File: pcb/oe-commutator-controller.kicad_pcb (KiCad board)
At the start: 4 copper layers, 43 x 95 mm, 93 parts, among them J1 0015910100, J2 USB4110-GF-A, J3 1719730004, SW1 SW_Push, U1 W25Q128JVS, U2 RP2040, U3 NCP1117-3.3_SOT223, U4 CAP1296-x-AIA, U5 PTN04050CAZ, U6 LTC4425, U7 TMC2130-LA, U8 IS31FL3193, Y1 ABM8AIG-12.000MHZ-12-2Z-T3

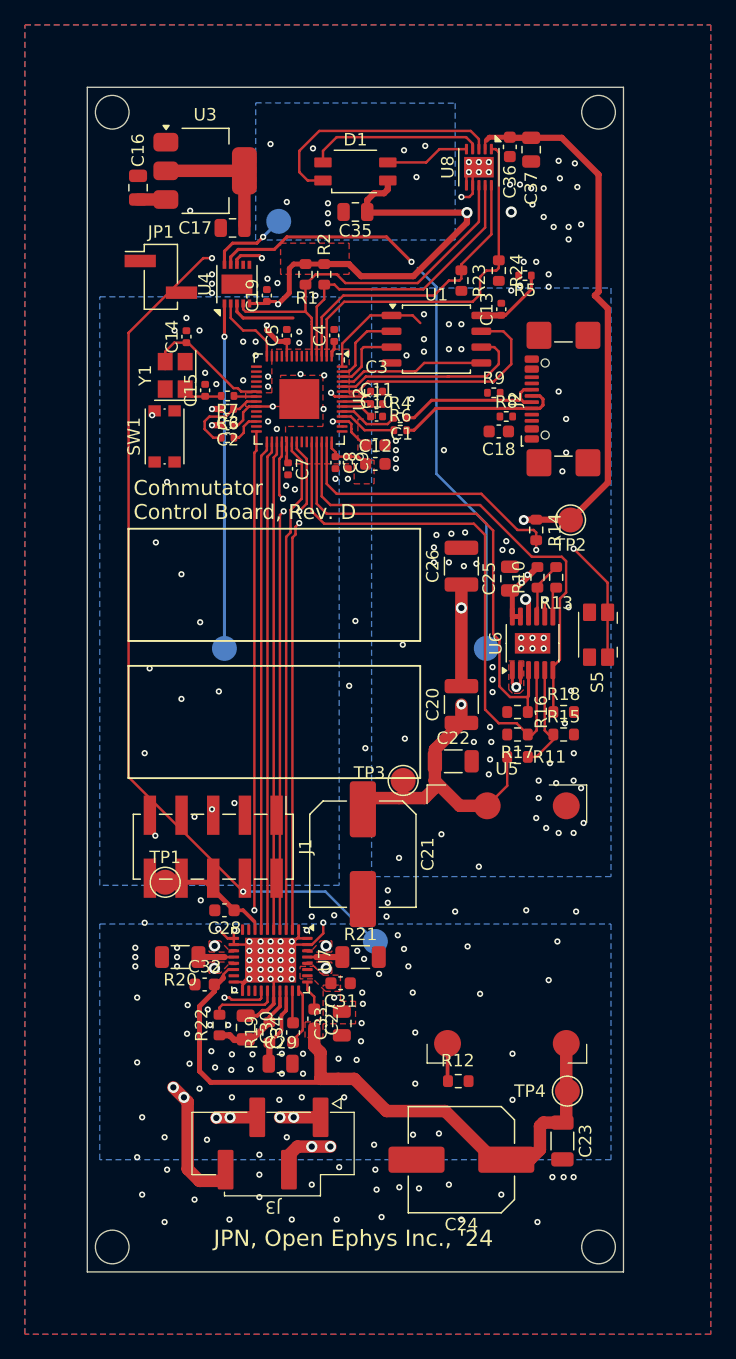
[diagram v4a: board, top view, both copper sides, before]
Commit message: Rev D PCB WIP for Review
- Before going into further minutiae, get review
- Components are laid out and routed
- Fails DRC check, requires vias for better GND plane, there are traces
  in the outer keepout zone, remove S5?
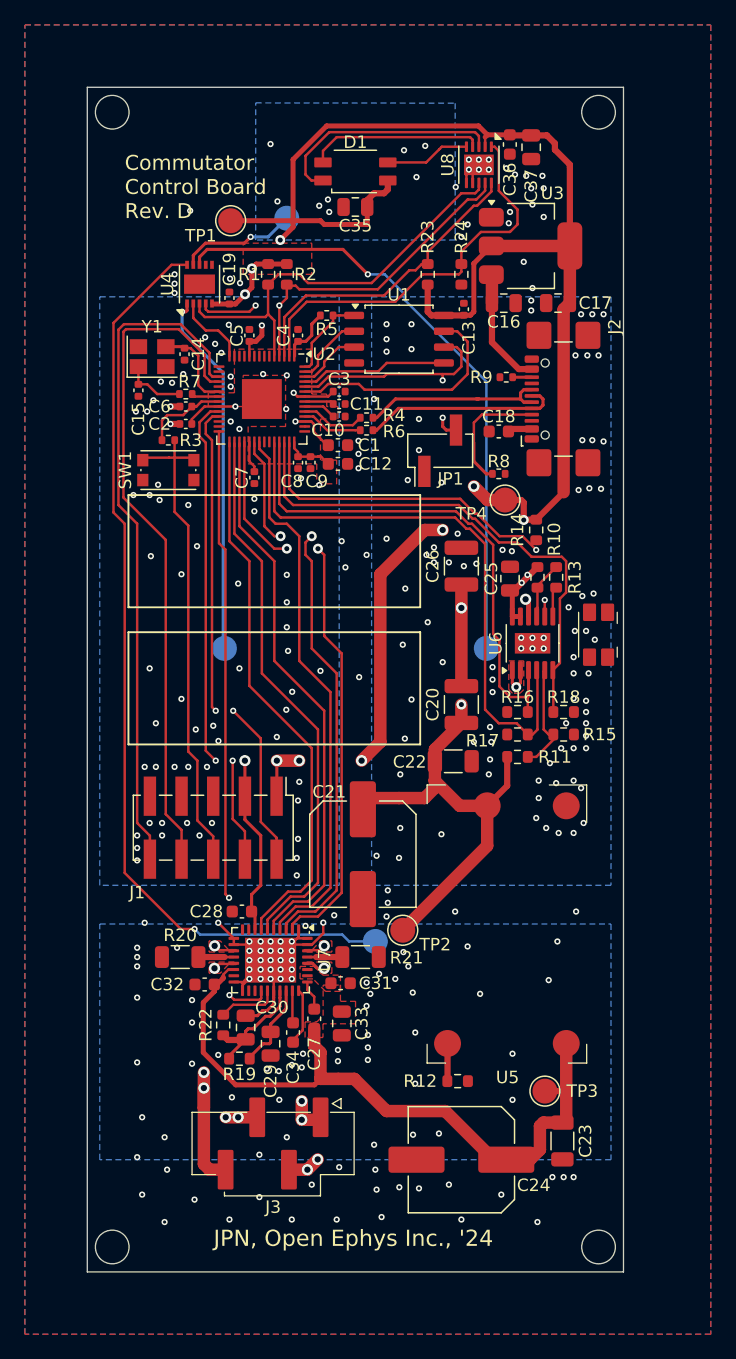
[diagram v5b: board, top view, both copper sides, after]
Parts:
- D1: footprint open-ephys:SUNLED_PLCC4-INV_3.2x2.8x1.9mm -> oe:SUNLED_PLCC4-INV_3.2x2.8x1.9mm
- S5: footprint open-ephys:PANASONIC_EVQP7-JA-01P -> oe:PANASONIC_EVQP7-JA-01P
- moved TP1 53.3 mm to (113.5, 64.7)
- moved TP4 47.7 mm to (135.5, 87.1)
- moved TP2 35.5 mm to (127.3, 121.6)
- moved C16 30.8 mm to (135.4, 71.3), turned to 0 degrees
- moved TP3 27.4 mm to (138.7, 134.5)
- moved U3 26.8 mm to (137.6, 66.7)
- moved C17 26.8 mm to (139.8, 71.3)
- moved JP1 26.4 mm to (130.3, 83.1), turned to 90 degrees
- moved R5 16.2 mm to (121.2, 72.3), turned to 0 degrees
- moved C15 5.35 mm to (106.1, 78.3), turned to -90 degrees
- moved R3 4.75 mm to (108.5, 82.3)
- moved R8 4.64 mm to (135.0, 85.0), turned to 180 degrees
- moved C6 3.36 mm to (109.9, 79.6)
- moved R7 3.35 mm to (109.9, 78.6)
- moved C2 3.35 mm to (109.9, 81.0)
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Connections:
- S1 pad 1: /Touch Sensors/CCW -> /Touch Sensors/CW
- S3 pad 1: /Touch Sensors/CW -> /Touch Sensors/CCW
- U2 pad 17: unconnected-(U2-GPIO14-Pad17) -> /MCU/GPIO_{1}
- U2 pad 18: unconnected-(U2-GPIO15-Pad18) -> /MCU/GPIO_{0}
- U2 pad 24: Net-(J1-Pin_2) -> Net-(J1-Pin_4)
- U2 pad 25: Net-(J1-Pin_4) -> Net-(J1-Pin_2)
- U2 pad 36: /MCU/GPIO_{0} -> unconnected-(U2-GPIO24-Pad36)
- U2 pad 37: /MCU/GPIO_{1} -> unconnected-(U2-GPIO25-Pad37)
- U4 pad 10: /Touch Sensors/MODE -> /Touch Sensors/STOP
- U4 pad 8: /Touch Sensors/STOP -> /Touch Sensors/CW
- U4 pad 9: /Touch Sensors/CW -> /Touch Sensors/MODE
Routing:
- net +3.3V: track 145.2 -> 210.5 mm, vias 10 -> 13
- net /MCU/GPIO_{1}: track 0.00 -> 54.8 mm, vias 2 -> 0
- net /MCU/GPIO_{0}: track 0.00 -> 54.7 mm
- net Net-(J1-Pin_2): track 0.00 -> 39.4 mm, vias 0 -> 2
- net Net-(J1-Pin_4): track 0.00 -> 39.3 mm, vias 1 -> 2
- net /MCU/~{RESET}: track 2.63 -> 39.0 mm, vias 1 -> 0
- net /Touch Sensors/CW: track 16.6 -> 50.6 mm
- net (no net): track 27.7 -> 0.00 mm, vias 4 -> 0
- net +5V: track 30.3 -> 43.1 mm, vias 3 -> 2
- net /MCU/IS31_{BM}: track 35.5 -> 25.0 mm
- net Net-(J2-CC1): track 0.00 -> 9.92 mm
- net Net-(S5-A): track 9.83 -> 0.00 mm, vias 1 -> 0
- net VBUS: track 2.25 -> 11.2 mm
- net /MCU/SCL: track 24.5 -> 32.9 mm
- net /MCU/SDA: track 24.4 -> 32.3 mm, vias 0 -> 2
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- added copper zone on B.Cu, net /Touch Sensors/CCW
- added copper zone on B.Cu, net /Touch Sensors/CW
- added copper zone on B.Cu, net /Touch Sensors/MODE
- added copper zone on B.Cu, net /Touch Sensors/STOP
- removed copper zone on B.Cu, net (none)
- removed copper zone on B.Cu, net /MCU/IS31_{EN}
- removed copper zone on B.Cu, net /MCU/SCL
- removed copper zone on B.Cu, net /MCU/SDA
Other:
- board text added: "Commutator Control Board Rev. D"
- board text removed: "Commutator Control Board, Rev. D"

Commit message: Revision D of controller PCB
- Small changes during PCB review
- This commit will be fabricated
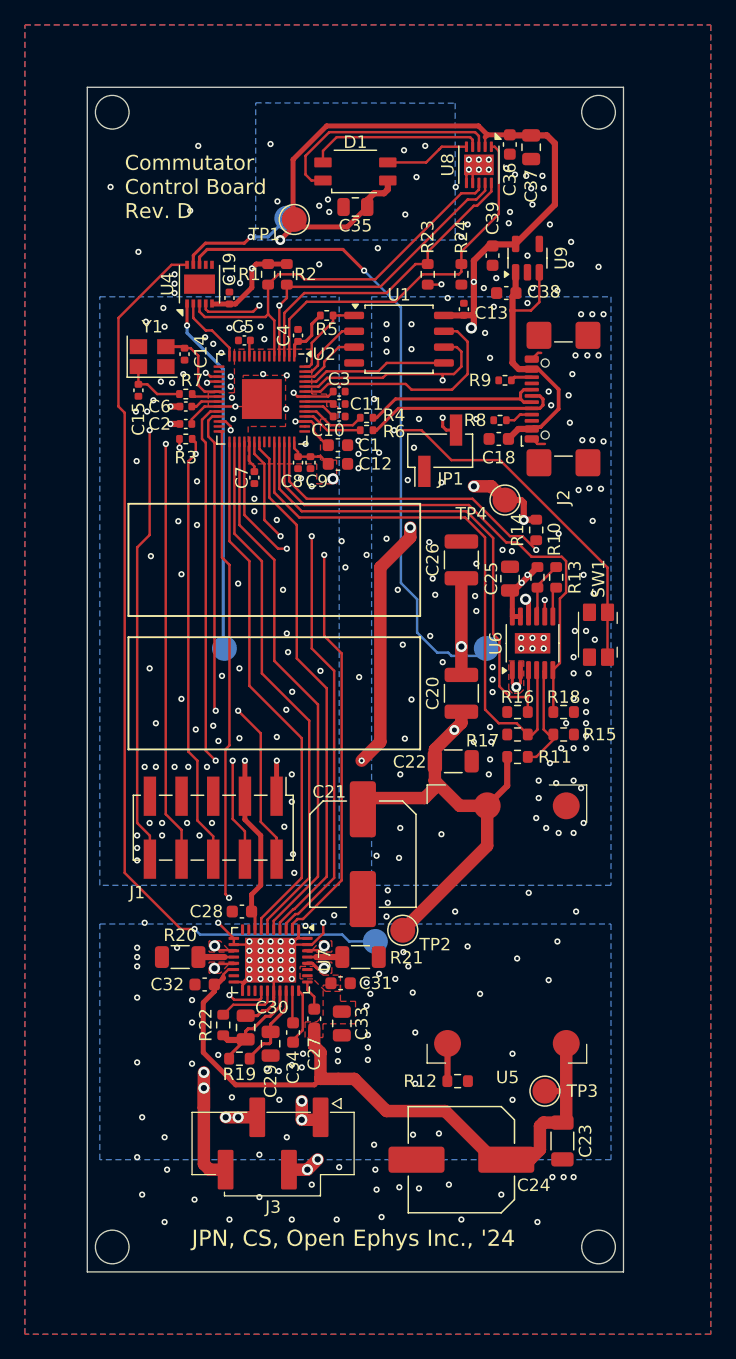
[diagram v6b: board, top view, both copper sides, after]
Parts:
- removed C16, C17: 10u, Capacitor_SMD:C_0805_2012Metric
- removed S5: EVQ-P7J01P, oe:PANASONIC_EVQP7-JA-01P
- removed U3: NCP1117-3.3_SOT223, Package_TO_SOT_SMD:SOT-223-3_TabPin2
- added C38: 1uF, Capacitor_SMD:C_0603_1608Metric, F.Cu at (135.6, 70.5)
- added C39: 1uF, Capacitor_SMD:C_0603_1608Metric, F.Cu at (134.5, 67.5)
- added U9: AP2112K-3.3, Package_TO_SOT_SMD:SOT-23-5, F.Cu at (137.3, 67.7)
- SW1: value SW_Push -> SW_MEC_5E; footprint Button_Switch_SMD:SW_Push_1P1T_NO_CK_KMR2 -> oe:PANASONIC_EVQP7-JA-01P
- moved SW1 36.9 mm to (143.0, 97.9), turned to -90 degrees
- moved TP1 5.10 mm to (118.6, 64.6)
- moved R8 4.30 mm to (135.1, 80.7), turned to 0 degrees
- moved R3 1.40 mm to (109.9, 82.2)
- moved C20 0.90 mm to (132.0, 102.6)
- moved C18 0.60 mm to (135.0, 82.2)
- moved C5 0.57 mm to (114.6, 74.3), turned to 180 degrees
- moved C26 0.50 mm to (132.0, 91.9)
- moved R9 0.27 mm to (135.5, 77.5)
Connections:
- SW1 pad 2: /MCU/~{RESET} -> GND
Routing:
- net /MCU/~{RESET}: track 39.0 -> 82.4 mm, vias 0 -> 3
- net /MCU/GPIO_{0}: track 54.7 -> 41.1 mm, vias 0 -> 2
- net VBUS: track 11.2 -> 23.4 mm
- net /MCU/GPIO_{1}: track 54.8 -> 43.6 mm, vias 0 -> 2
- net Net-(J2-CC1): track 9.92 -> 2.22 mm
- net +3.3V: track 210.5 -> 203.8 mm, vias 13 -> 16
- net /MCU/IS31_{EN}: track 32.6 -> 30.0 mm
- net GND: track 31.6 -> 33.8 mm, vias 299 -> 329
- net /MCU/SCLK: track 46.4 -> 44.8 mm
- net /Touch Sensors/CW: track 50.6 -> 52.1 mm
- net /MCU/MOSI: track 44.4 -> 42.9 mm
- net /MCU/TMC_{DIR}: track 44.0 -> 42.8 mm
- net /MCU/TMC_{STEP}: track 44.1 -> 42.9 mm
- net /MCU/MISO: track 44.2 -> 43.1 mm
- net +5V: track 43.1 -> 43.9 mm
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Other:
- board text added: "JPN, CS, Open Ephys Inc., '24"
- board text removed: "JPN, Open Ephys Inc., '24"
